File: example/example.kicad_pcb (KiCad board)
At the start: 4 copper layers, 80 x 49 mm, 124 parts, among them J1 USB_B_Micro, J2 Conn_02x10_Odd_Even, J3 Conn_02x10_Odd_Even, J4 Conn_01x02, U1 CY7C68013A-56LTX, U10 DAC081C081CIMK, U11 TPS73101DBV, U12 ADC081C021CIMM, U13 DAC081C081CIMK, U14 TPS73101DBV, U15 TPD3S014, U2 CAT24M01W, U3 CAT24C256W, U4 ICE40UP5K-SG48ITR, U5 FXMA108BQX, U6 FXMA108BQX, U7 LM3880MF-1AF, U8 MIC5355-S4YMME, U9 ADC081C021CIMM, Y1 24M

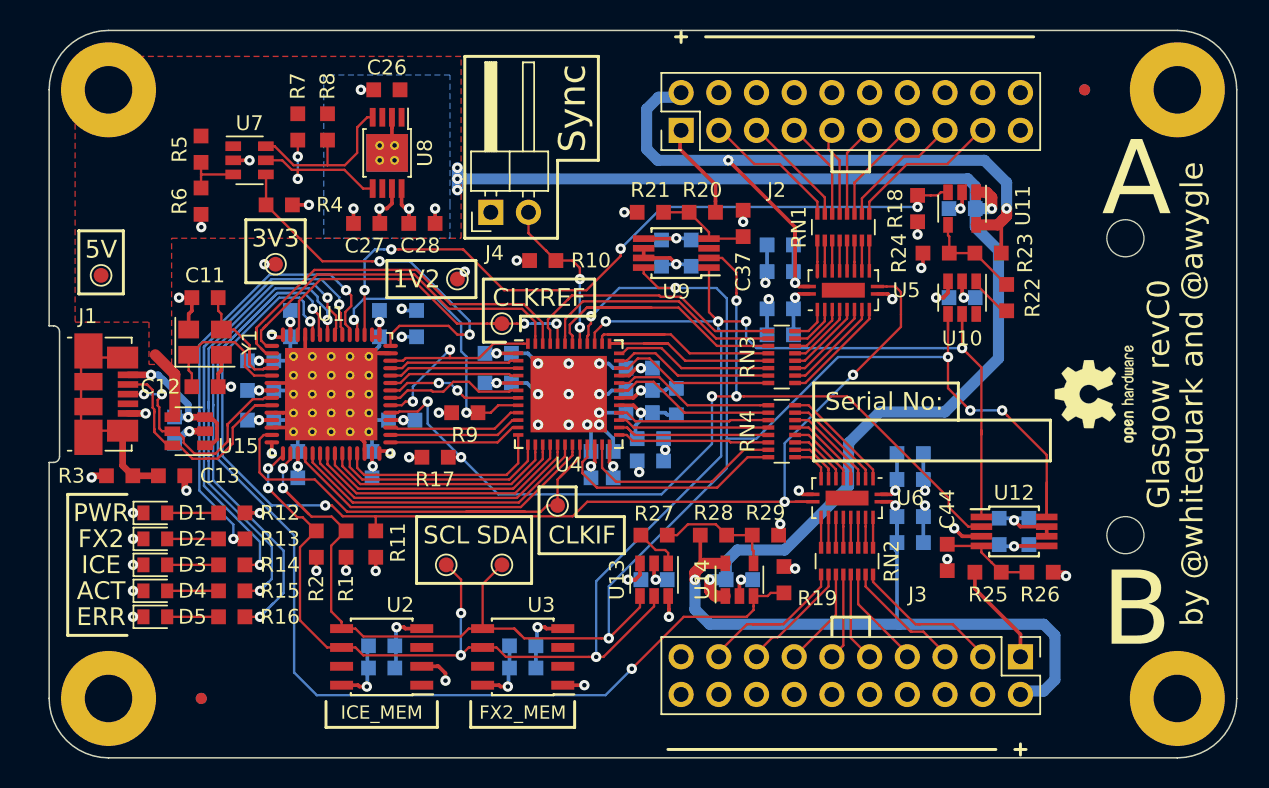
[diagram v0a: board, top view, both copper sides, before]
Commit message: Update example to Glasgow revC3.
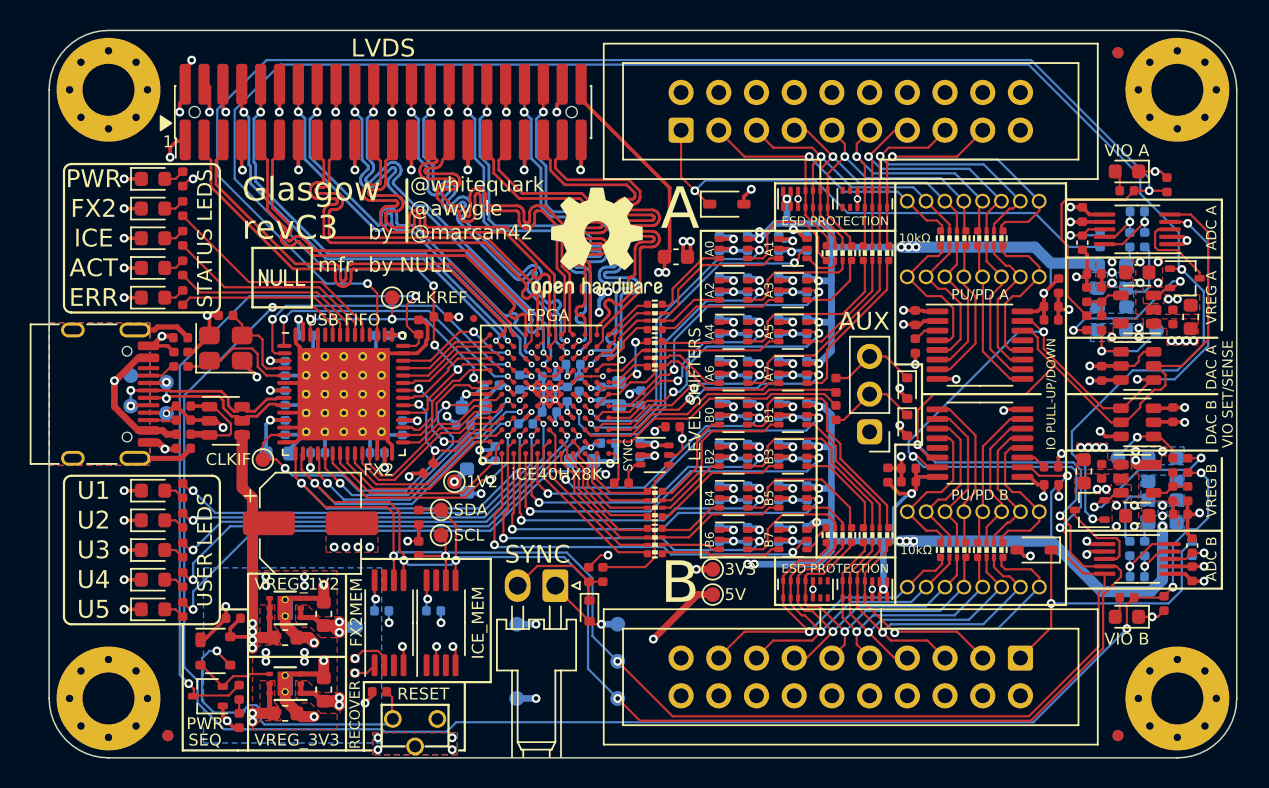
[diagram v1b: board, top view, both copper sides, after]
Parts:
- removed MK5, MK6: Mounting_Hole, MountingHole:MountingHole_2.5mm
- removed the REF** at (120.5, 95.5)
- added C48: u1, Capacitor_SMD:C_0402_1005Metric, B.Cu at (99.2, 93.8)
- added C49: u1, Capacitor_SMD:C_0402_1005Metric, B.Cu at (101.0, 85.3)
- added C50: u1, Capacitor_SMD:C_0402_1005Metric, B.Cu at (101.0, 88.2)
- added C51: u1, Capacitor_SMD:C_0402_1005Metric, B.Cu at (101.0, 91.0)
- added C52: u1, Capacitor_SMD:C_0402_1005Metric, B.Cu at (101.0, 93.8)
- added C53: 4u7, Capacitor_SMD:C_0603_1608Metric, F.Cu at (123.3, 103.7)
- added C54: u1, Capacitor_SMD:C_0402_1005Metric, F.Cu at (117.5, 89.6)
- added C55: u1, Capacitor_SMD:C_0402_1005Metric, F.Cu at (119.6, 83.4)
- added C56: u1, Capacitor_SMD:C_0402_1005Metric, F.Cu at (120.9, 94.1)
- added C57: u1, Capacitor_SMD:C_0402_1005Metric, F.Cu at (120.4, 87.4)
- added C58: u1, Capacitor_SMD:C_0402_1005Metric, B.Cu at (123.3, 83.2)
- added C59: u1, Capacitor_SMD:C_0402_1005Metric, F.Cu at (125.7, 90.3)
- added C60: u1, Capacitor_SMD:C_0402_1005Metric, B.Cu at (95.2, 96.5)
- added C61: u1, Capacitor_SMD:C_0402_1005Metric, B.Cu at (95.2, 99.3)
- added C62: u1, Capacitor_SMD:C_0402_1005Metric, B.Cu at (95.2, 102.2)
- added C63: u1, Capacitor_SMD:C_0402_1005Metric, B.Cu at (95.2, 105.0)
- added C64: u1, Capacitor_SMD:C_0402_1005Metric, B.Cu at (97.0, 96.5)
- added C65: u1, Capacitor_SMD:C_0402_1005Metric, B.Cu at (97.0, 99.3)
- added C66: u1, Capacitor_SMD:C_0402_1005Metric, B.Cu at (97.0, 102.2)
- added C67: u1, Capacitor_SMD:C_0402_1005Metric, B.Cu at (97.0, 105.0)
- added C68: u1, Capacitor_SMD:C_0402_1005Metric, B.Cu at (99.2, 96.5)
- added C69: u1, Capacitor_SMD:C_0402_1005Metric, B.Cu at (99.2, 99.3)
- added C70: u1, Capacitor_SMD:C_0402_1005Metric, B.Cu at (99.2, 102.2)
- added C71: u1, Capacitor_SMD:C_0402_1005Metric, B.Cu at (99.2, 105.0)
- added C72: u1, Capacitor_SMD:C_0402_1005Metric, B.Cu at (101.0, 96.5)
- added C73: u1, Capacitor_SMD:C_0402_1005Metric, B.Cu at (101.0, 99.3)
- added C74: u1, Capacitor_SMD:C_0402_1005Metric, B.Cu at (101.0, 102.2)
- added C75: u1, Capacitor_SMD:C_0402_1005Metric, B.Cu at (101.0, 105.0)
- added C76: 4u7, Capacitor_SMD:C_0603_1608Metric, B.Cu at (78.6, 96.4)
- added C77: u1, Capacitor_SMD:C_0402_1005Metric, B.Cu at (84.9, 95.5)
- added C78: u1, Capacitor_SMD:C_0402_1005Metric, B.Cu at (79.8, 94.9)
- added C79: u1, Capacitor_SMD:C_0402_1005Metric, B.Cu at (87.2, 95.5)
- added C80: 4u7, Capacitor_SMD:C_0603_1608Metric, B.Cu at (88.4, 95.5)
- added C81: u1, Capacitor_SMD:C_0402_1005Metric, B.Cu at (80.0, 99.5)
- added C82: 4u7, Capacitor_SMD:C_0603_1608Metric, F.Cu at (126.9, 90.3)
- added C83: 4u7, Capacitor_SMD:C_0603_1608Metric, F.Cu at (123.3, 87.3)
- added C84: u1, Capacitor_SMD:C_0402_1005Metric, F.Cu at (108.3, 90.3)
- added C85: u1, Capacitor_SMD:C_0402_1005Metric, B.Cu at (89.8, 99.2)
- added C86: 4u7, Capacitor_SMD:C_0603_1608Metric, F.Cu at (65.9, 111.9)
- added C87: 150u, Capacitor_SMD:CP_Elec_6.3x5.9, F.Cu at (67.6, 104.2)
- added C88: u1, Capacitor_SMD:C_0402_1005Metric, F.Cu at (74.9, 91.0)
- added C89: u1, Capacitor_SMD:C_0402_1005Metric, F.Cu at (72.2, 115.5)
- added C90: 1n 50V C0G, Capacitor_SMD:C_0402_1005Metric, F.Cu at (127.0, 105.7)
- added C91: 1n 50V C0G, Capacitor_SMD:C_0402_1005Metric, F.Cu at (119.6, 85.3)
- added C92: 4u7, Capacitor_SMD:C_0603_1608Metric, F.Cu at (92.2, 86.2)
- added D10: BLU, LED_SMD:LED_0603_1608Metric, F.Cu at (57.0, 110.0)
- added D11: ESD5Z5.0T1G, Glasgow:D_SOD-523, F.Cu at (86.4, 110.1)
- added D12: ESD5Z5.0T1G, Glasgow:D_SOD-523, F.Cu at (107.8, 97.6)
- added D13: ESD5Z5.0T1G, Glasgow:D_SOD-523, F.Cu at (107.8, 95.1)
- added D14: GRN, LED_SMD:LED_0603_1608Metric, F.Cu at (122.6, 110.5)
- added D15: GRN, LED_SMD:LED_0603_1608Metric, F.Cu at (122.6, 80.5)
- added D16: CDSOD323-T36S, Glasgow:D_SOD-323, F.Cu at (116.3, 106.0)
- added D17: CDSOD323-T36S, Glasgow:D_SOD-323, F.Cu at (95.7, 82.7)
- added D18: BAT54CW, Glasgow:SOT-323_SC-70, F.Cu at (120.1, 103.3)
- added D19: BAT54CW, Glasgow:SOT-323_SC-70, F.Cu at (126.5, 87.7)
- added D20: SP3012-06UTG, Glasgow:UDFN-14_3.5x1.35mm_P0.5mm, F.Cu at (105.0, 108.7)
- added D21: SP3012-06UTG, Glasgow:UDFN-14_3.5x1.35mm_P0.5mm, F.Cu at (101.0, 108.7)
- added D22: SP3012-06UTG, Glasgow:UDFN-14_3.5x1.35mm_P0.5mm, F.Cu at (101.0, 82.3)
- added D23: SP3012-06UTG, Glasgow:UDFN-14_3.5x1.35mm_P0.5mm, F.Cu at (105.0, 82.3)
- added D24: BAT54AW, Glasgow:SOT-323_SC-70, F.Cu at (60.7, 115.8)
- added D6: BLU, LED_SMD:LED_0603_1608Metric, F.Cu at (57.0, 102.0)
- added D7: PNK, LED_SMD:LED_0603_1608Metric, F.Cu at (57.0, 104.0)
- added D8: WHT, LED_SMD:LED_0603_1608Metric, F.Cu at (57.0, 106.0)
- added D9: PNK, LED_SMD:LED_0603_1608Metric, F.Cu at (57.0, 108.0)
- added FB1: 600R, 0.5A, Inductor_SMD:L_0402_1005Metric, F.Cu at (59.0, 98.2)
- added FID3: Fiducial_0.75mm_Mask1.5mm, Fiducial:Fiducial_0.75mm_Mask1.5mm, F.Cu at (122.0, 118.5)
- added FID6: Fiducial_0.75mm_Mask1.5mm, Fiducial:Fiducial_0.75mm_Mask1.5mm, B.Cu at (122.0, 118.5)
- added FID8: Fiducial_0.5mm_Dia_1mm_Outer, Fiducial:Fiducial_0.5mm_Dia_1mm_Outer, F.Cu at (78.6, 90.4)
- added J10: AUX, Connector_PinHeader_2.54mm:PinHeader_1x03_P2.54mm_Vertical, F.Cu at (105.3, 98.0)
- added J5: PinHeader_2x22_P1.27mm, Glasgow:PinHeader_2x22_P1.27mm_Vertical__SMD, F.Cu at (72.5, 76.5)
- added J6: Conn_01x08, Glasgow:PinSocket_1x08_P1.27mm_Vertical_DNP, F.Cu at (116.7, 108.5)
- added J7: Conn_01x08, Glasgow:PinSocket_1x08_P1.27mm_Vertical_DNP, F.Cu at (116.7, 103.4)
- added J8: Conn_01x08, Glasgow:PinSocket_1x08_P1.27mm_Vertical_DNP, F.Cu at (107.8, 82.5)
- added J9: Conn_01x08, Glasgow:PinSocket_1x08_P1.27mm_Vertical_DNP, F.Cu at (107.8, 87.6)
- added NONO_HANA: MECHOKKU, Glasgow:nono_hana_lines, B.Cu at (73.8, 82.5)
- added R31: 100R, Resistor_SMD:R_0402_1005Metric, B.Cu at (77.9, 97.6)
- added R32: 100R, Resistor_SMD:R_0402_1005Metric, B.Cu at (89.8, 95.8)
- added R33: 49k9, Resistor_SMD:R_0402_1005Metric, F.Cu at (120.9, 90.7)
- added R34: 59k, Resistor_SMD:R_0402_1005Metric, F.Cu at (120.9, 88.8)
- added R35: 24k3, Resistor_SMD:R_0402_1005Metric, F.Cu at (119.9, 88.8)
- added R36: 10k, Resistor_SMD:R_0402_1005Metric, F.Cu at (117.5, 100.4)
- added R37: 10k, Resistor_SMD:R_0402_1005Metric, F.Cu at (108.3, 92.2)
- added R38: 47R, Resistor_SMD:R_0402_1005Metric, F.Cu at (87.3, 107.7)
- added R39: 47R, Resistor_SMD:R_0402_1005Metric, F.Cu at (103.0, 96.8)
- added R40: DNP, Glasgow:R_0402_1005Metric_DNP, F.Cu at (70.6, 113.8)
- added R41: 2k2, Resistor_SMD:R_0402_1005Metric, F.Cu at (107.9, 100.5)
- added R42: 2k2, Resistor_SMD:R_0402_1005Metric, F.Cu at (117.5, 90.5)
- added R43: 47R, Resistor_SMD:R_0402_1005Metric, F.Cu at (103.0, 94.9)
- added R44: 10k, Resistor_SMD:R_0402_1005Metric, F.Cu at (86.3, 107.7)
- added R45: 47R, Resistor_SMD:R_0402_1005Metric, F.Cu at (88.5, 101.5)
- added R46: 20k, Resistor_SMD:R_0402_1005Metric, F.Cu at (122.6, 109.2)
- added R47: 20k, Resistor_SMD:R_0402_1005Metric, F.Cu at (122.6, 81.8)
- added R48: 0R15, Resistor_SMD:R_0603_1608Metric, B.Cu at (124.0, 103.4)
- added R49: 0R15, Resistor_SMD:R_0603_1608Metric, B.Cu at (122.5, 87.6)
- added R50: DNP, Glasgow:R_0603_1608Metric_DNP, B.Cu at (126.0, 103.4)
- added R51: DNP, Glasgow:R_0603_1608Metric_DNP, B.Cu at (120.7, 87.6)
- added R52: 5k1, Resistor_SMD:R_0402_1005Metric, F.Cu at (59.0, 97.2)
- added R53: 5k1, Resistor_SMD:R_0402_1005Metric, F.Cu at (58.4, 93.2)
- added R54: 4R7, Resistor_SMD:R_0402_1005Metric, B.Cu at (122.8, 85.1)
- added R55: 10k, Resistor_SMD:R_0402_1005Metric, F.Cu at (119.9, 90.7)
- added R56: 0R33, Resistor_SMD:R_0603_1608Metric, B.Cu at (122.5, 90.4)
- added R57: 2k2, Resistor_SMD:R_0402_1005Metric, F.Cu at (106.5, 101.0)
- added R58: 2k2, Resistor_SMD:R_0402_1005Metric, F.Cu at (118.0, 88.2)
- added R59: 470, Resistor_SMD:R_0402_1005Metric, B.Cu at (127.0, 105.9)
- added R60: 470, Resistor_SMD:R_0402_1005Metric, B.Cu at (120.8, 85.1)
- added REF**: OSHW-Logo2_9.8x8mm_SilkScreen, Symbol:OSHW-Logo2_9.8x8mm_SilkScreen, F.Cu at (86.9, 85.3)
- added REF**: null_Logo_SilkS_4mm, Glasgow:null_Logo_SilkS_4mm, F.Cu at (65.7, 87.7)
- added REF**: Tab, kikit:Tab, F.Cu at (120.0, 70.5)
- added REF**: Tab, kikit:Tab, F.Cu at (60.0, 120.5)
- added REF**: Tab, kikit:Tab, F.Cu at (60.0, 70.6)
- added REF**: Tab, kikit:Tab, F.Cu at (120.0, 120.5)
- added REF**: null_Logo_SilkS_6mm, Glasgow:null_Logo_SilkS_6mm, B.Cu at (59.5, 107.0)
- added RN10: 33R, Glasgow:R_Array_Convex_4x0402, F.Cu at (105.7, 86.0)
- added RN11: 10k, Glasgow:R_Array_Convex_4x0402, F.Cu at (110.9, 85.0)
- added RN12: 10k, Glasgow:R_Array_Convex_4x0402, F.Cu at (113.4, 85.0)
- added RN5: 10k, Glasgow:R_Array_Convex_4x0402, F.Cu at (113.4, 106.0)
- added RN6: 10k, Glasgow:R_Array_Convex_4x0402, F.Cu at (110.9, 106.0)
- added RN7: 33R, Glasgow:R_Array_Convex_4x0402, F.Cu at (90.8, 90.3)
- added RN8: 33R, Glasgow:R_Array_Convex_4x0402, F.Cu at (90.8, 92.8)
- added RN9: 33R, Glasgow:R_Array_Convex_4x0402, F.Cu at (103.2, 86.0)
- added SW1: RST, Glasgow:SW_Tactile_SPST_Angled_TC-1109DE, F.Cu at (74.7, 117.4)
- added TP10: SDA, TestPoint:TestPoint_Pad_D1.0mm, B.Cu at (88.3, 116.0)
- added TP11: SCL, TestPoint:TestPoint_Pad_D1.0mm, B.Cu at (88.3, 113.5)
- added TP12: GND, TestPoint:TestPoint_Pad_D1.0mm, B.Cu at (88.3, 111.0)
- added TP13: VBUS, TestPoint:TestPoint_Pad_D1.0mm, B.Cu at (55.5, 94.2)
- added TP14: USBGND, TestPoint:TestPoint_Pad_D1.0mm, B.Cu at (57.9, 96.8)
- added TP15: USBDP, TestPoint:TestPoint_Pad_D1.0mm, B.Cu at (55.5, 96.3)
- added TP16: USBDM, TestPoint:TestPoint_Pad_D1.0mm, B.Cu at (57.9, 94.7)
- added TP17: 1V2, TestPoint:TestPoint_Pad_D1.0mm, B.Cu at (70.7, 111.2)
- added TP18: VDAC, TestPoint:TestPoint_Pad_D1.0mm, B.Cu at (122.0, 99.8)
- added TP19: VDAC, TestPoint:TestPoint_Pad_D1.0mm, B.Cu at (124.6, 91.2)
- added TP8: 5V, TestPoint:TestPoint_Pad_D1.0mm, B.Cu at (81.5, 116.0)
- added TP9: 3V3, TestPoint:TestPoint_Pad_D1.0mm, B.Cu at (81.5, 111.0)
- added U16: SN74LVC1T45DCKR, Glasgow:SOT-363_SC-70-6, F.Cu at (100.1, 88.5)
- added U17: SN74LVC1T45DCKR, Glasgow:SOT-363_SC-70-6, F.Cu at (100.1, 91.3)
- added U18: SN74LVC1T45DCKR, Glasgow:SOT-363_SC-70-6, F.Cu at (100.1, 94.1)
- added U19: PCA6408APW, Package_SO:TSSOP-16_4.4x5mm_P0.65mm, F.Cu at (112.7, 92.2)
- added U20: DAC081C081CIMK, Glasgow:SOT-23-6, F.Cu at (123.3, 93.6)
- added U21: INA233, Glasgow:VSSOP-10_3x3mm_P0.5mm, F.Cu at (123.3, 84.4)
- added U22: SN74LVC1T45DCKR, Glasgow:SOT-363_SC-70-6, F.Cu at (96.1, 96.9)
- added U23: SN74LVC1T45DCKR, Glasgow:SOT-363_SC-70-6, F.Cu at (96.1, 99.7)
- added U24: SN74LVC1T45DCKR, Glasgow:SOT-363_SC-70-6, F.Cu at (96.1, 102.5)
- added U25: SN74LVC1T45DCKR, Glasgow:SOT-363_SC-70-6, F.Cu at (96.1, 105.3)
- added U26: SN74LVC1T45DCKR, Glasgow:SOT-363_SC-70-6, F.Cu at (100.1, 96.9)
- added U27: SN74LVC1T45DCKR, Glasgow:SOT-363_SC-70-6, F.Cu at (100.1, 99.7)
- added U28: SN74LVC1T45DCKR, Glasgow:SOT-363_SC-70-6, F.Cu at (100.1, 102.5)
- added U29: SN74LVC1T45DCKR, Glasgow:SOT-363_SC-70-6, F.Cu at (100.1, 105.3)
- added U30: ICE40HX8K-BG121, Package_BGA:BGA-121_9.0x9.0mm_Layout11x11_P0.8mm_Ball0.4mm_Pad0.35mm_NSMD, F.Cu at (83.7, 95.5)
- added U31: TPS73101DBV, Glasgow:SOT-23-5, F.Cu at (123.3, 89.8)
- added U32: SN74LVC1T45DCKR, Glasgow:SOT-363_SC-70-6, F.Cu at (90.8, 99.6)
- added U36: TLV73312PQDRVR, Glasgow:DFN-6-1EP_2x2mm_P0.65mm_EP1x1.6mm_ThermalVias, F.Cu at (65.9, 109.9)
- C1, C14, C19, C26, C27, C28: footprint Capacitor_SMD:C_0603_1608Metric_Pad0.99x1.00mm_HandSolder -> Capacitor_SMD:C_0603_1608Metric
- C10, C13, C15, C17, C2, C20, C21, C23, C24, C25, C3, C33, C35, C36, C38, C4, C40, C42, C43, C47, C5, C6, C7, C9: footprint Capacitor_SMD:C_0603_1608Metric_Pad0.99x1.00mm_HandSolder -> Capacitor_SMD:C_0402_1005Metric
- C11, C12: value 18p -> 9p; footprint Capacitor_SMD:C_0603_1608Metric_Pad0.99x1.00mm_HandSolder -> Capacitor_SMD:C_0402_1005Metric
- C16, C29, C46: value 4u7 -> u1; footprint Capacitor_SMD:C_0603_1608Metric_Pad0.99x1.00mm_HandSolder -> Capacitor_SMD:C_0402_1005Metric; moved to F.Cu
- C18, C34, C39, C41: value 4u7 -> u1; footprint Capacitor_SMD:C_0603_1608Metric_Pad0.99x1.00mm_HandSolder -> Capacitor_SMD:C_0402_1005Metric
- C22, C30, C32, C45, C8: footprint Capacitor_SMD:C_0603_1608Metric_Pad0.99x1.00mm_HandSolder -> Capacitor_SMD:C_0402_1005Metric; moved to F.Cu
- C31: footprint Capacitor_SMD:C_0603_1608Metric_Pad0.99x1.00mm_HandSolder -> Capacitor_SMD:C_0603_1608Metric; moved to F.Cu
- C37, C44: value 12n -> u1; footprint Capacitor_SMD:C_0603_1608Metric_Pad0.99x1.00mm_HandSolder -> Capacitor_SMD:C_0402_1005Metric; moved to B.Cu
- D1, D5: footprint LED_SMD:LED_0603_1608Metric_Pad0.82x1.00mm_HandSolder -> LED_SMD:LED_0603_1608Metric
- D2: value GRN -> WHT; footprint LED_SMD:LED_0603_1608Metric_Pad0.82x1.00mm_HandSolder -> LED_SMD:LED_0603_1608Metric
- D3: value GRN -> BLU; footprint LED_SMD:LED_0603_1608Metric_Pad0.82x1.00mm_HandSolder -> LED_SMD:LED_0603_1608Metric
- D4: value YEL -> ORA; footprint LED_SMD:LED_0603_1608Metric_Pad0.82x1.00mm_HandSolder -> LED_SMD:LED_0603_1608Metric
- FID1, FID2: value Fiducial_0.75mm_Dia_1.5mm_Outer -> Fiducial_0.75mm_Mask1.5mm; footprint Fiducial:Fiducial_0.75mm_Dia_1.5mm_Outer -> Fiducial:Fiducial_0.75mm_Mask1.5mm
- FID4: renamed from FID1; value Fiducial_0.75mm_Dia_1.5mm_Outer -> Fiducial_0.75mm_Mask1.5mm; footprint Fiducial:Fiducial_0.75mm_Dia_1.5mm_Outer -> Fiducial:Fiducial_0.75mm_Mask1.5mm
- FID5: renamed from FID4; value Fiducial_0.75mm_Dia_1.5mm_Outer -> Fiducial_0.75mm_Mask1.5mm; footprint Fiducial:Fiducial_0.75mm_Dia_1.5mm_Outer -> Fiducial:Fiducial_0.75mm_Mask1.5mm
- J1: value USB_B_Micro -> USB_C_USB2.0; footprint Connector_USB:USB_Micro-B_Molex_47346-0001 -> Glasgow:USB_C_Receptacle_HRO_TYPE-C-31-M-12
- J2, J3: value Conn_02x10_Odd_Even -> IDC-Header_2x10_P2.54mm; footprint Connector_PinHeader_2.54mm:PinHeader_2x10_P2.54mm_Vertical -> Connector_IDC:IDC-Header_2x10_P2.54mm_Vertical
- J4: footprint Connector_PinHeader_2.54mm:PinHeader_1x02_P2.54mm_Horizontal -> Glasgow:Molex_KK-254_1x02_P2.54mm_Horizontal
- MK1, MK2, MK3, MK4: footprint MountingHole:MountingHole_3.2mm_M3_Pad -> Glasgow:MountingHole_3.5mm_Pad_Via_CrtYd
- R1, R13, R14, R17, R2, R26, R27, R28, R29, R4, R9: footprint Resistor_SMD:R_0603_1608Metric_Pad0.99x1.00mm_HandSolder -> Resistor_SMD:R_0402_1005Metric
- R10: value 390 -> 2k2; footprint Resistor_SMD:R_0603_1608Metric_Pad0.99x1.00mm_HandSolder -> Resistor_SMD:R_0402_1005Metric
- R11: value 100k -> 2k2; footprint Resistor_SMD:R_0603_1608Metric_Pad0.99x1.00mm_HandSolder -> Resistor_SMD:R_0402_1005Metric
- R12: value 2k2 -> 10k; footprint Resistor_SMD:R_0603_1608Metric_Pad0.99x1.00mm_HandSolder -> Resistor_SMD:R_0402_1005Metric
- R15: value 390 -> 1k; footprint Resistor_SMD:R_0603_1608Metric_Pad0.99x1.00mm_HandSolder -> Resistor_SMD:R_0402_1005Metric
- R16: value 604 -> 1k; footprint Resistor_SMD:R_0603_1608Metric_Pad0.99x1.00mm_HandSolder -> Resistor_SMD:R_0402_1005Metric
- R18, R19: value 100k -> 10k; footprint Resistor_SMD:R_0603_1608Metric_Pad0.99x1.00mm_HandSolder -> Resistor_SMD:R_0402_1005Metric
- R20, R21: value 10k -> 2k2; footprint Resistor_SMD:R_0603_1608Metric_Pad0.99x1.00mm_HandSolder -> Resistor_SMD:R_0402_1005Metric
- R22: value 49k9 -> 2k2; footprint Resistor_SMD:R_0603_1608Metric_Pad0.99x1.00mm_HandSolder -> Resistor_SMD:R_0402_1005Metric
- R23: value 59k -> 2k2; footprint Resistor_SMD:R_0603_1608Metric_Pad0.99x1.00mm_HandSolder -> Resistor_SMD:R_0402_1005Metric
- R24: value 24k3 -> 4R7; footprint Resistor_SMD:R_0603_1608Metric_Pad0.99x1.00mm_HandSolder -> Resistor_SMD:R_0402_1005Metric; moved to B.Cu
- R25: value 10k -> 4R7; footprint Resistor_SMD:R_0603_1608Metric_Pad0.99x1.00mm_HandSolder -> Resistor_SMD:R_0402_1005Metric; moved to B.Cu
- R3: value 1M -> 100k; footprint Resistor_SMD:R_0603_1608Metric_Pad0.99x1.00mm_HandSolder -> Resistor_SMD:R_0402_1005Metric
- R30: value 100 -> 4R7; footprint Resistor_SMD:R_0603_1608Metric_Pad0.99x1.00mm_HandSolder -> Resistor_SMD:R_0402_1005Metric
- R5: value 220k -> 100k; footprint Resistor_SMD:R_0603_1608Metric_Pad0.99x1.00mm_HandSolder -> Resistor_SMD:R_0402_1005Metric
- R6, R8: value 100k -> DNP; footprint Resistor_SMD:R_0603_1608Metric_Pad0.99x1.00mm_HandSolder -> Glasgow:R_0603_1608Metric_DNP; moved to B.Cu
- R7: value 100k -> 0R33; footprint Resistor_SMD:R_0603_1608Metric_Pad0.99x1.00mm_HandSolder -> Resistor_SMD:R_0603_1608Metric; moved to B.Cu
- RN1, RN2, RN3, RN4: value R_Pack08 -> 33R; footprint Resistor_SMD:R_Array_Convex_8x0602 -> Glasgow:R_Array_Convex_4x0402
- U10: value DAC081C081CIMK -> SN74LVC1T45DCKR; footprint Package_TO_SOT_SMD:SOT-23-6 -> Glasgow:SOT-363_SC-70-6
- U11: value TPS73101DBV -> SN74LVC1T45DCKR; footprint Package_TO_SOT_SMD:SOT-23-5 -> Glasgow:SOT-363_SC-70-6
- U12: value ADC081C021CIMM -> INA233; footprint Package_SO:MSOP-8_3x3mm_P0.65mm -> Glasgow:VSSOP-10_3x3mm_P0.5mm
- U13, U15: footprint Package_TO_SOT_SMD:SOT-23-6 -> Glasgow:SOT-23-6
- U14: footprint Package_TO_SOT_SMD:SOT-23-5 -> Glasgow:SOT-23-5
- U2: value CAT24M01W -> CAT24M01X; footprint Package_SO:SOIC-8_3.9x4.9mm_P1.27mm -> Package_SO:TSSOP-8_4.4x3mm_P0.65mm
- U3: value CAT24C256W -> BL24C256A-SFRC; footprint Package_SO:SOIC-8_3.9x4.9mm_P1.27mm -> Package_SO:TSSOP-8_4.4x3mm_P0.65mm
- U4: value ICE40UP5K-SG48ITR -> SN74LVC1T45DCKR; footprint Package_DFN_QFN:QFN-48-1EP_7x7mm_P0.5mm_EP5.15x5.15mm -> Glasgow:SOT-363_SC-70-6
- U5: value FXMA108BQX -> PCA6408APW; footprint Package_DFN_QFN:WQFN-20-1EP_2.5x4.5mm_P0.5mm_EP1x2.9mm -> Package_SO:TSSOP-16_4.4x5mm_P0.65mm
- U6: value FXMA108BQX -> SN74LVC1T45DCKR; footprint Package_DFN_QFN:WQFN-20-1EP_2.5x4.5mm_P0.5mm_EP1x2.9mm -> Glasgow:SOT-363_SC-70-6
- U7: value LM3880MF-1AF -> APX811-40UG-7; footprint Package_TO_SOT_SMD:SOT-23-6 -> Glasgow:SOT-143
- U8: value MIC5355-S4YMME -> TLV75533PDRVR; footprint Package_SO:MSOP-8-1EP_3x3mm_P0.65mm_EP2.54x2.8mm_ThermalVias -> Glasgow:DFN-6-1EP_2x2mm_P0.65mm_EP1x1.6mm_ThermalVias
- U9: value ADC081C021CIMM -> SN74LVC1T45DCKR; footprint Package_SO:MSOP-8_3x3mm_P0.65mm -> Glasgow:SOT-363_SC-70-6
- Y1: footprint Crystals:Crystal_SMD_3225-4pin_3.2x2.5mm -> Glasgow:Crystal_SMD_3225-4Pin_3.2x2.5mm
- moved R6 68.2 mm to (126.0, 100.6), turned to -90 degrees
- moved R7 61.8 mm to (124.0, 100.6), turned to -90 degrees
- moved R23 59.3 mm to (59.0, 110.0), turned to -90 degrees
- moved R22 58.7 mm to (59.0, 108.0), turned to -90 degrees
- moved R8 53.5 mm to (120.7, 90.4)
- moved TP1 46.5 mm to (94.7, 109.0)
- moved C26 42.6 mm to (65.9, 117.0)
- moved R20 40.7 mm to (59.0, 104.0), turned to -90 degrees
- moved R21 38.9 mm to (59.0, 106.0), turned to -90 degrees
- moved C22 38.3 mm to (117.5, 101.6)
- moved R5 36.7 mm to (62.8, 115.6)
- moved U8 36.4 mm to (65.9, 115.0), turned to 180 degrees
- moved TP3 35.9 mm to (94.7, 107.3)
- moved R27 35.3 mm to (125.7, 100.3), turned to -90 degrees
- moved R4 34.8 mm to (62.8, 117.5), turned to 90 degrees
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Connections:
- net /IOBufferB/VFB renamed /IO_Banks/IO_Buffer_B/VFB
- net Net-(R27-Pad1) renamed /IO_Banks/IO_Buffer_B/VDAC
- C14 pad 1: +3V3 -> +1V2
- C16 pad 1: +3V3 -> +5V
- C18 pad 1: /VCCPLL -> +1V2
- C26 pad 1: +5V -> GND
- C26 pad 2: GND -> +5V
- C29 pad 1: +3V3 -> /IO_Banks/VIOB
- C31 pad 1: +3V3 -> +5V
- C33 pad 1: /VCCPLL -> /IO_Banks/VIO_AUX
- C37 pad 1: /IOBufferA/VSAMP -> +3V3
- C38 pad 1: +5V -> /IO_Banks/VIOA
- C39 pad 1: /IOBufferA/VIO -> /IO_Banks/VIOA
- C40 pad 1: /IOBufferA/VIO -> /IO_Banks/VIOA
- C41 pad 1: +3V3 -> /IO_Banks/VIOA
- C44 pad 1: /IOBufferB/VSAMP -> Net-(U12-Vin-)
- C44 pad 2: GND -> Net-(U12-Vin+)
- C46 pad 1: /IOBufferB/VIO -> /IO_Banks/VIOB
- C47 pad 1: /IOBufferB/VIO -> +3V3
- J2 pad 1: /IOBufferA/VSENSE -> /IO_Banks/IO_Buffer_A/VSENSE
- J2 pad 11: /IOBufferA/Z4 -> /IO_Banks/IO_Buffer_A/Z4
- J2 pad 13: /IOBufferA/Z5 -> /IO_Banks/IO_Buffer_A/Z5
- J2 pad 15: /IOBufferA/Z6 -> /IO_Banks/IO_Buffer_A/Z6
- J2 pad 17: /IOBufferA/Z7 -> /IO_Banks/IO_Buffer_A/Z7
- J2 pad 19: Net-(J2-Pad19) -> unconnected-(J2-Pin_19-Pad19)
- J2 pad 2: /IOBufferA/VIO -> /IO_Banks/VIOA
- J2 pad 20: GND -> unconnected-(J2-Pin_20-Pad20)
- J2 pad 3: /IOBufferA/Z0 -> /IO_Banks/IO_Buffer_A/Z0
- J2 pad 5: /IOBufferA/Z1 -> /IO_Banks/IO_Buffer_A/Z1
- J2 pad 7: /IOBufferA/Z2 -> /IO_Banks/IO_Buffer_A/Z2
- J2 pad 9: /IOBufferA/Z3 -> /IO_Banks/IO_Buffer_A/Z3
- J3 pad 1: /IOBufferB/VSENSE -> /IO_Banks/IO_Buffer_B/VSENSE
- J3 pad 11: /IOBufferB/Z4 -> /IO_Banks/IO_Buffer_B/Z4
- J3 pad 13: /IOBufferB/Z5 -> /IO_Banks/IO_Buffer_B/Z5
- J3 pad 15: /IOBufferB/Z6 -> /IO_Banks/IO_Buffer_B/Z6
- J3 pad 17: /IOBufferB/Z7 -> /IO_Banks/IO_Buffer_B/Z7
- J3 pad 19: Net-(J3-Pad19) -> unconnected-(J3-Pin_19-Pad19)
- J3 pad 2: /IOBufferB/VIO -> /IO_Banks/VIOB
- J3 pad 20: GND -> unconnected-(J3-Pin_20-Pad20)
- J3 pad 3: /IOBufferB/Z0 -> /IO_Banks/IO_Buffer_B/Z0
- J3 pad 5: /IOBufferB/Z1 -> /IO_Banks/IO_Buffer_B/Z1
- J3 pad 7: /IOBufferB/Z2 -> /IO_Banks/IO_Buffer_B/Z2
- J3 pad 9: /IOBufferB/Z3 -> /IO_Banks/IO_Buffer_B/Z3
- J4 pad 2: /~SYNC -> /IO_Banks/~{SYNC}
- R10 pad 1: /~SYNC -> Net-(U30A-IOT_219)
- R10 pad 2: +3V3 -> GND
- R11 pad 1: /~OEQ -> /IO_Banks/U1
- R11 pad 2: +3V3 -> Net-(D6-A)
- R17 pad 1: /~ALERT -> /~{ALERT}
- R20 pad 1: /IOBufferA/VSAMP -> /IO_Banks/U2
- R20 pad 2: /IOBufferA/VSENSE -> Net-(D7-A)
- R21 pad 1: GND -> /IO_Banks/U3
- R21 pad 2: /IOBufferA/VSAMP -> Net-(D8-A)
- R22 pad 1: Net-(R22-Pad1) -> /IO_Banks/U4
- R22 pad 2: /IOBufferA/VFB -> Net-(D9-A)
- R23 pad 1: /IOBufferA/VFB -> /IO_Banks/U5
- R23 pad 2: /IOBufferA/VIO -> Net-(D10-A)
- R24 pad 1: GND -> /IO_Banks/IO_Buffer_B/ISNS_H
- R24 pad 2: /IOBufferA/VFB -> Net-(U12-Vin+)
- R25 pad 1: /IOBufferB/VSAMP -> /IO_Banks/VIOB
- R25 pad 2: /IOBufferB/VSENSE -> Net-(U12-Vin-)
- R26 pad 1: GND -> /IO_Banks/IO_Buffer_B/VIO_EN
- R26 pad 2: /IOBufferB/VSAMP -> /ENVB
- R28 pad 2: /IOBufferB/VIO -> /IO_Banks/VIOB
- R30 pad 1: /VCCPLL -> /IO_Banks/IO_Buffer_A/ISNS_H
- R30 pad 2: +1V2 -> Net-(U21-Vin+)
- R4 pad 1: /~CY_RESET -> +3V3
- R4 pad 2: +3V3 -> Net-(R4-Pad2)
- R5 pad 1: /PGOOD -> Net-(R4-Pad2)
- R5 pad 2: +5V -> /~{CY_RESET}
- R6 pad 1: GND -> Net-(U14-OUT)
- R6 pad 2: /PGOOD -> /IO_Banks/IO_Buffer_B/ISNS_H
- R7 pad 1: /3V3EN -> Net-(U14-OUT)
- R7 pad 2: +5V -> /IO_Banks/IO_Buffer_B/ISNS_H
- R8 pad 1: /1V2EN -> Net-(U31-OUT)
- R8 pad 2: +5V -> /IO_Banks/IO_Buffer_A/ISNS_H
- R9 pad 2: /~FPGA_RESET -> /~{FPGA_RESET}
- RN1 pad 1: /IOBufferA/Y0 -> /IO_Banks/QB0
- RN1 pad 2: /IOBufferA/Y1 -> /IO_Banks/QB1
- RN1 pad 3: /IOBufferA/Y2 -> /IO_Banks/QB2
- RN1 pad 4: /IOBufferA/Y3 -> /IO_Banks/QB3
- RN1 pad 5: /IOBufferA/Y4 -> /IO_Banks/IO_Buffer_B/X3
- RN1 pad 6: /IOBufferA/Y5 -> /IO_Banks/IO_Buffer_B/X2
- RN1 pad 7: /IOBufferA/Y6 -> /IO_Banks/IO_Buffer_B/X1
- RN1 pad 8: /IOBufferA/Y7 -> /IO_Banks/IO_Buffer_B/X0
- RN2 pad 1: /IOBufferB/Y0 -> /IO_Banks/QB4
- RN2 pad 2: /IOBufferB/Y1 -> /IO_Banks/QB5
- RN2 pad 3: /IOBufferB/Y2 -> /IO_Banks/QB6
- RN2 pad 4: /IOBufferB/Y3 -> /IO_Banks/QB7
- RN2 pad 5: /IOBufferB/Y4 -> /IO_Banks/IO_Buffer_B/X7
- RN2 pad 6: /IOBufferB/Y5 -> /IO_Banks/IO_Buffer_B/X6
- RN2 pad 7: /IOBufferB/Y6 -> /IO_Banks/IO_Buffer_B/X5
- RN2 pad 8: /IOBufferB/Y7 -> /IO_Banks/IO_Buffer_B/X4
- RN3 pad 1: /QA0 -> /IO_Banks/IO_Buffer_B/Y0
- RN3 pad 2: /QA1 -> /IO_Banks/IO_Buffer_B/Y1
- RN3 pad 3: /QA2 -> /IO_Banks/IO_Buffer_B/Y2
- RN3 pad 4: /QA3 -> /IO_Banks/IO_Buffer_B/Y3
- RN3 pad 5: /QA4 -> /IO_Banks/IO_Buffer_B/Z3
- RN3 pad 6: /QA5 -> /IO_Banks/IO_Buffer_B/Z2
- RN3 pad 7: /QA6 -> /IO_Banks/IO_Buffer_B/Z1
- RN3 pad 8: /QA7 -> /IO_Banks/IO_Buffer_B/Z0
- RN4 pad 1: /QB0 -> /IO_Banks/IO_Buffer_B/Y4
- RN4 pad 2: /QB1 -> /IO_Banks/IO_Buffer_B/Y5
- RN4 pad 3: /QB2 -> /IO_Banks/IO_Buffer_B/Y6
- RN4 pad 4: /QB3 -> /IO_Banks/IO_Buffer_B/Y7
- RN4 pad 5: /QB4 -> /IO_Banks/IO_Buffer_B/Z7
- RN4 pad 6: /QB5 -> /IO_Banks/IO_Buffer_B/Z6
- RN4 pad 7: /QB6 -> /IO_Banks/IO_Buffer_B/Z5
- RN4 pad 8: /QB7 -> /IO_Banks/IO_Buffer_B/Z4
- U1 pad 33: /~ALERT -> /~{ALERT}
- U1 pad 34: /FLAGD -> /~{FPGA_RESET}
- U1 pad 42: /~CY_RESET -> /~{CY_RESET}
- U1 pad 46: /~FPGA_RESET -> unconnected-(U1-PD1/FD9-Pad46)
- U1 pad 52: /~OEQ -> unconnected-(U1-PD7/FD15-Pad52)
- U10 pad 1: Net-(R22-Pad1) -> +3V3
- U10 pad 2: +3V3 -> GND
- U10 pad 3: GND -> /IO_Banks/IO_Buffer_A/X6
- U10 pad 4: /SDA -> /IO_Banks/IO_Buffer_A/Y6
- U10 pad 5: /SCL -> /IO_Banks/DA6
- U10 pad 6: /IOBufferA/ADRDAC -> /IO_Banks/VIOA
- U11 pad 1: +5V -> +3V3
- U11 pad 3: /ENVA -> /IO_Banks/IO_Buffer_A/X1
- U11 pad 4: /IOBufferA/VFB -> /IO_Banks/IO_Buffer_A/Y1
- U11 pad 5: /IOBufferA/VIO -> /IO_Banks/DA1
- U12 pad 1: /SCL -> GND
- U12 pad 2: /~ALERT -> +3V3
- U12 pad 3: GND -> Net-(U12-~{Alert})
- U12 pad 4: /IOBufferB/VSAMP -> /SDA
- U12 pad 5: +3V3 -> /SCL
- U12 pad 6: GND -> +3V3
- U12 pad 8: /SDA -> Net-(U12-Vbus)
- U14 pad 3: /ENVB -> /IO_Banks/IO_Buffer_B/VIO_EN
- U14 pad 5: /IOBufferB/VIO -> Net-(U14-OUT)
- U15 pad 5: /USB_P -> /USB_N
- U15 pad 6: /USB_N -> /USB_P
- U2 pad 1: Net-(U2-Pad1) -> unconnected-(U2-NC-Pad1)
- U2 pad 3: Net-(U2-Pad3) -> unconnected-(U2-A2-Pad3)
- U2 pad 7: Net-(U2-Pad7) -> unconnected-(U2-WP-Pad7)
- U3 pad 3: Net-(U3-Pad3) -> unconnected-(U3-A2-Pad3)
- U3 pad 7: Net-(U3-Pad7) -> unconnected-(U3-WP-Pad7)
- U4 pad 2: /PKTEND -> GND
- U4 pad 3: /A1 -> /IO_Banks/IO_Buffer_A/X0
- U4 pad 4: /A0 -> /IO_Banks/IO_Buffer_A/Y0
- U4 pad 5: +1V2 -> /IO_Banks/DA0
- U4 pad 6: /OE -> /IO_Banks/VIOA
- U5 pad 10: GND -> /IO_Banks/IO_Buffer_B/P5
- U5 pad 11: /~OEQ -> /IO_Banks/IO_Buffer_B/P6
- U5 pad 12: /IOBufferA/Y7 -> /IO_Banks/IO_Buffer_B/P7
- U5 pad 13: /IOBufferA/Y6 -> unconnected-(U5-~{INT}-Pad13)
- U5 pad 14: /IOBufferA/Y5 -> /SCL
- U5 pad 15: /IOBufferA/Y4 -> /SDA
- U5 pad 16: /IOBufferA/Y3 -> /IO_Banks/VIOB
- U5 pad 2: /IOBufferA/X0 -> /IO_Banks/VIOB
- U5 pad 3: /IOBufferA/X1 -> Net-(U5-~{RESET})
- U5 pad 4: /IOBufferA/X2 -> /IO_Banks/IO_Buffer_B/P0
- U5 pad 5: /IOBufferA/X3 -> /IO_Banks/IO_Buffer_B/P1
- U5 pad 6: /IOBufferA/X4 -> /IO_Banks/IO_Buffer_B/P2
- U5 pad 7: /IOBufferA/X5 -> /IO_Banks/IO_Buffer_B/P3
- U5 pad 8: /IOBufferA/X6 -> GND
- U5 pad 9: /IOBufferA/X7 -> /IO_Banks/IO_Buffer_B/P4
- U6 pad 2: /IOBufferB/X0 -> GND
- U6 pad 3: /IOBufferB/X1 -> /IO_Banks/IO_Buffer_A/X2
- U6 pad 4: /IOBufferB/X2 -> /IO_Banks/IO_Buffer_A/Y2
- U6 pad 5: /IOBufferB/X3 -> /IO_Banks/DA2
- U6 pad 6: /IOBufferB/X4 -> /IO_Banks/VIOA
- U7 pad 1: +5V -> GND
- U7 pad 2: GND -> Net-(U7-~{RESET})
- U7 pad 3: /PGOOD -> /~{MR}
- U7 pad 4: /~CY_RESET -> +5V
- U8 pad 1: +5V -> +3V3
- U8 pad 2: GND -> +3V3
- U8 pad 3: Net-(U8-Pad3) -> GND
- U8 pad 4: /1V2EN -> Net-(U7-~{RESET})
- U8 pad 5: /3V3EN -> +5V
- U8 pad 6: Net-(U8-Pad6) -> +5V
- U8 pad 7: +1V2 -> GND
- U9 pad 1: /SCL -> +3V3
- U9 pad 2: /~ALERT -> GND
- U9 pad 3: /IOBufferA/ADRADC -> /IO_Banks/IO_Buffer_A/X4
- U9 pad 4: /IOBufferA/VSAMP -> /IO_Banks/IO_Buffer_A/Y4
- U9 pad 5: +3V3 -> /IO_Banks/DA4
- U9 pad 6: GND -> /IO_Banks/VIOA
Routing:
- net GND: track 113.8 -> 255.8 mm, vias 57 -> 121
- net /~{ALERT}: track 0.00 -> 133.8 mm, vias 0 -> 5
- net /IO_Banks/VIOB: track 0.00 -> 120.4 mm, vias 0 -> 19
- net /IO_Banks/VIOA: track 0.00 -> 99.3 mm, vias 0 -> 17
- net /~OEQ: track 79.8 -> 0.00 mm, vias 4 -> 0
- net /~ALERT: track 63.8 -> 0.00 mm, vias 5 -> 0
- net /ENVA: track 49.4 -> 105.3 mm, vias 4 -> 2
- net /IOBufferA/VIO: track 51.5 -> 0.00 mm, vias 3 -> 0
- net +5V: track 86.5 -> 136.9 mm, vias 5 -> 16
- net /IOBufferB/VIO: track 49.2 -> 0.00 mm, vias 2 -> 0
- net /~{CY_RESET}: track 0.00 -> 48.8 mm, vias 0 -> 2
- net +3V3: track 68.2 -> 114.0 mm, vias 33 -> 54
- net /SCL: track 121.2 -> 165.8 mm, vias 9 -> 7
- net /SDA: track 126.3 -> 166.8 mm, vias 8 -> 10
- net /IO_Banks/U5: track 0.00 -> 39.3 mm, vias 0 -> 3
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- added copper zone on F.Cu, net +1V2
- added copper zone on In2.Cu, net +1V2
- added copper zone on F.Cu, net +3V3
- added copper zone on B.Cu, net /IO_Banks/IO_Buffer_A/ISNS_H
- added copper zone on B.Cu, net /IO_Banks/IO_Buffer_B/ISNS_H
- added copper zone on B.Cu, net /IO_Banks/VIOA
- added copper zone on F.Cu, net /IO_Banks/VIOA
- added copper zone on B.Cu, net /IO_Banks/VIOB
- added copper zone on F.Cu, net /IO_Banks/VIOB
- added copper zone on B.Cu, net /SHLD
- added copper zone on F.Cu, net /SHLD
- added copper zone on In1.Cu, net /SHLD
- added copper zone on In2.Cu, net /SHLD
- added copper zone on B.Cu, net /SWSH
- added copper zone on F.Cu, net /SWSH
- added copper zone on In1.Cu, net /SWSH
- added copper zone on F.Cu, net GND
- added copper zone on B.Cu, net Net-(U14-OUT)
- added copper zone on F.Cu, net Net-(U14-OUT)
- added copper zone on B.Cu, net Net-(U31-OUT)
- added copper zone on F.Cu, net Net-(U31-OUT)
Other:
- outline, holes or cut-outs redrawn
- net class Default removed
- net class Power removed
- board text added: "0"
- board text added: "1"
- board text added: "10kΩ"
- board text added: "2"
- board text added: "3"
- board text added: "4"
- board text added: "5"
- board text added: "6"
- board text added: "7"
- board text added: "@whitequark @awygle @marcan42"
- board text added: "A 0"
- board text added: "A 1"
- board text added: "A 2"
- board text added: "A 3"
- board text added: "A 4"
- board text added: "A 5"
- board text added: "A 6"
- board text added: "A 7"
- board text added: "A0"
- board text added: "A1"
- board text added: "A2"
- board text added: "A3"
- board text added: "A4"
- board text added: "A5"
- board text added: "A6"
- board text added: "A7"
- board text added: "ADC A"
- board text added: "ADC B"
- board text added: "AUX"
- board text added: "B 0"
- board text added: "B 1"
- board text added: "B 2"
- board text added: "B 3"
- board text added: "B 4"
- board text added: "B 5"
- board text added: "B 6"
- board text added: "B 7"
- board text added: "B0"
- board text added: "B1"
- board text added: "B2"
- board text added: "B3"
- board text added: "B4"
- board text added: "B5"
- board text added: "B6"
- board text added: "B7"
- board text added: "Caution: Check washer & screw size for conflicts with LVDS connector"
- board text added: "D+"
- board text added: "D-"
- board text added: "DAC A"
- board text added: "DAC B"
- board text added: "ESD PROTECTION"
- board text added: "FPGA"
- board text added: "FX2MEM"
- board text added: "G"
- board text added: "GND"
- board text added: "Glasgow revC3"
- board text added: "IO PULL-UP/DOWN"
- board text added: "LEVEL SHIFTERS"
- board text added: "LVDS"
- board text added: "NULL"
- board text added: "PU/PD A"
- board text added: "PU/PD B"
- board text added: "Pull-Up/Down Resistors Bank A"
- board text added: "Pull-Up/Down Resistors Bank B"
- board text added: "RECOVER"
- board text added: "RESET"
- board text added: "S"
- board text added: "SEQ"
- board text added: "STATUS LEDS"
- board text added: "SYNC"
- board text added: "U1"
- board text added: "U2"
- board text added: "U3"
- board text added: "U4"
- board text added: "U5"
- board text added: "USB FIFO"
- board text added: "USER LEDS"
- board text added: "V"
- board text added: "VDAC"
- board text added: "VIO A"
- board text added: "VIO B"
- board text added: "VIO SET/SENSE"
- board text added: "VREG A"
- board text added: "VREG B"
- board text added: "VREG_1V2"
- board text added: "VREG_3V3"
- board text added: "VUSB"
- board text added: "Wave soldering keepout"
- board text added: "by"
- board text added: "https://glasgow-embedded.org"
- board text added: "iCE40HX8K"
- board text added: "manufactured by"
- board text added: "mfr."
- board text removed: "FX2_MEM"
- board text removed: "Glasgow revC0"
- board text removed: "Sync"
- board text removed: "by @whitequark and @awygle"
